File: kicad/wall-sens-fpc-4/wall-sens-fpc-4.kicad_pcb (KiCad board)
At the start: 2 copper layers, 51.5 x 19.7 mm, 32 parts, among them J1 10x0.5mm FPC, Q1 PT100MF0MP, Q2 PT100MF0MP, Q3 PT100MF0MP, Q4 PT100MF0MP, Q5 BC817, Q6 SSM3K122TU, Q7 BC817, Q8 SSM3K122TU

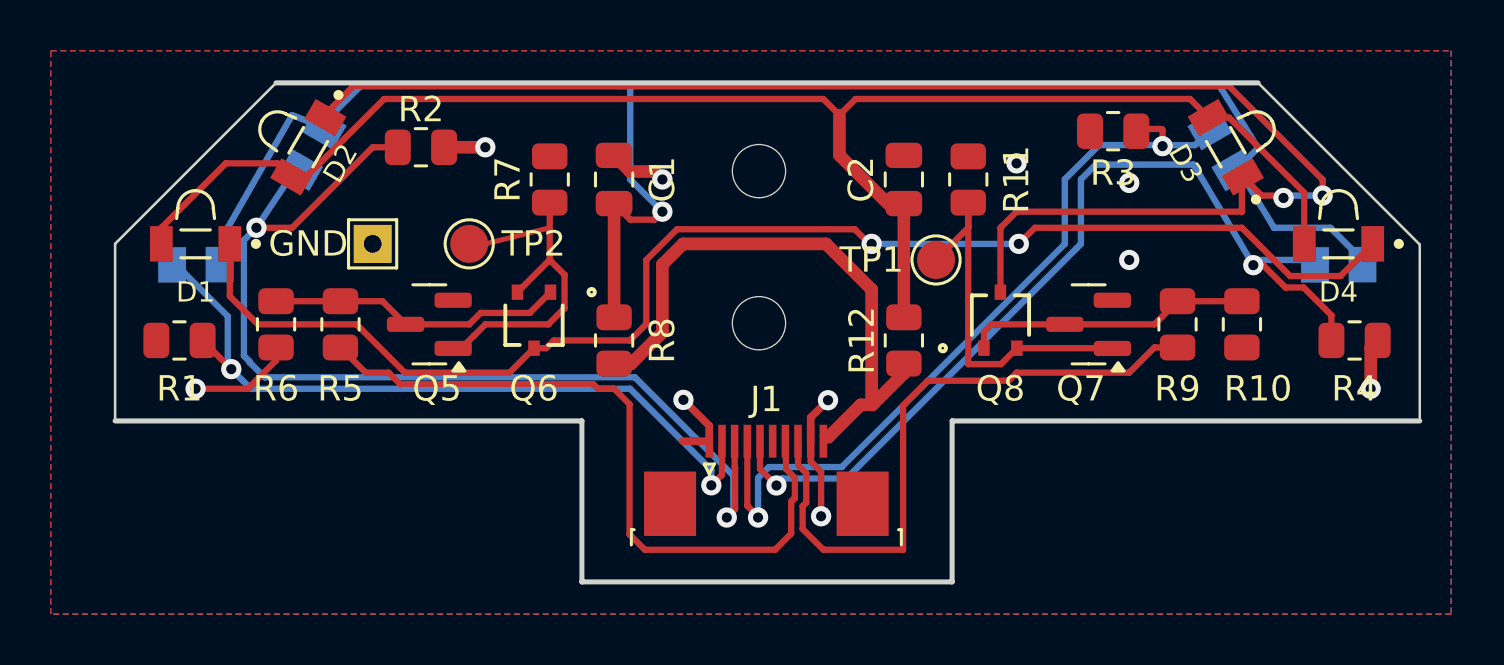
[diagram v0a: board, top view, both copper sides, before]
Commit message: New version of wall-follower for full size. Add new design Half-Monty-2
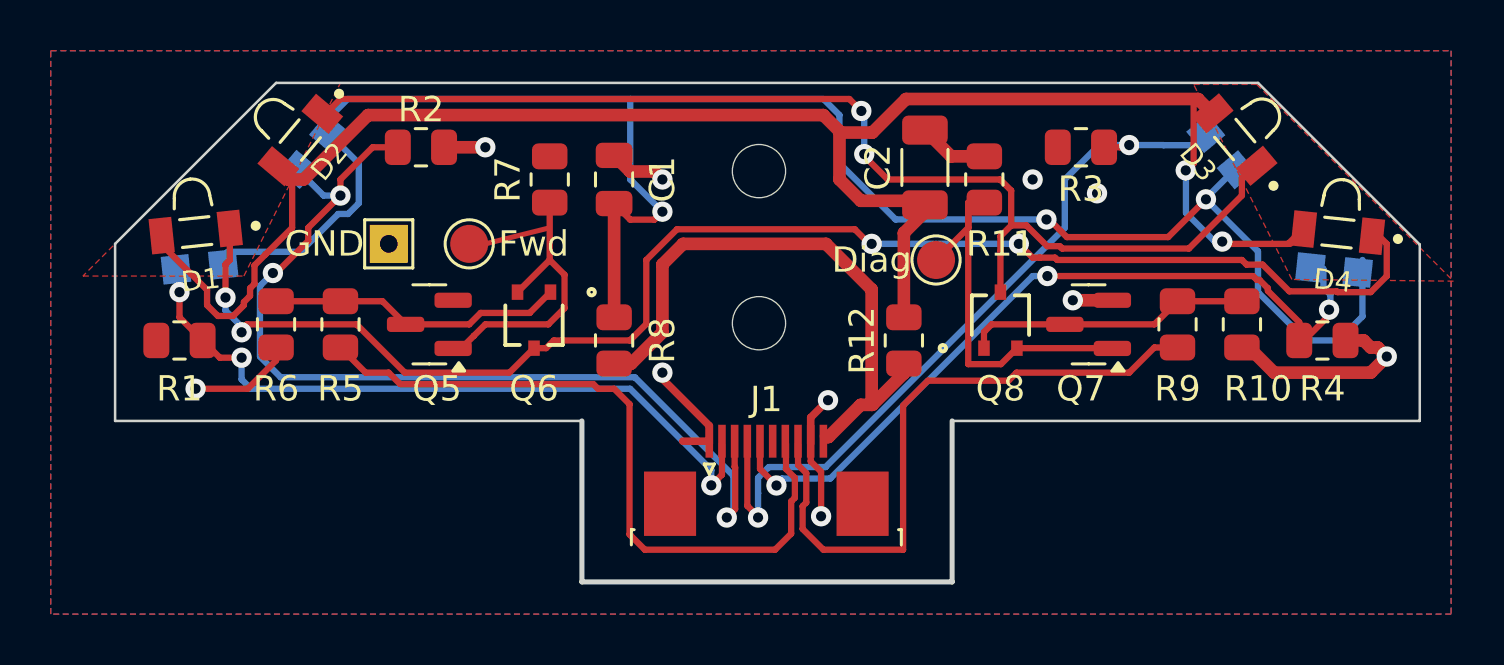
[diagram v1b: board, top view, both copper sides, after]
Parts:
- C2: value 22uF -> 47uF; footprint Capacitor_SMD:C_0805_2012Metric -> Capacitor_SMD:C_1206_3216Metric
- moved R3 1.42 mm to (164.5, 99.1)
- moved R4 1.27 mm to (174.0, 106.7)
- moved C2 0.96 mm to (158.3, 99.9)
- moved R11 0.63 mm to (160.7, 100.3)
- moved TP3 0.63 mm to (137.2, 102.9)
- moved D1 0.47 mm to (129.5, 102.4), turned to -174 degrees
- moved D3 0.47 mm to (170.5, 98.8), turned to 130 degrees
- moved D4 0.44 mm to (174.6, 102.4), turned to 174 degrees
- moved D2 0.43 mm to (133.7, 98.8), turned to -130 degrees
- moved Q4 0.21 mm to (174.5, 103.6), turned to 174 degrees
- moved Q1 0.12 mm to (129.7, 103.5), turned to -174 degrees
- turned Q2 to -130 degrees
- turned Q3 to 130 degrees
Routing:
- net Net-(D2-K): track 59.9 -> 46.6 mm
- net Net-(D1-A): track 61.7 -> 74.7 mm, vias 0 -> 2
- net GND: track 18.4 -> 30.4 mm
- net Net-(Q1-C): track 67.4 -> 74.7 mm, vias 1 -> 3
- net A3: track 37.1 -> 31.6 mm, vias 2 -> 3
- net Net-(D1-K): track 54.0 -> 57.7 mm, vias 2 -> 4
- net A1: track 41.1 -> 38.8 mm, vias 2 -> 3
- net A2: track 31.6 -> 30.5 mm
- net A0: track 29.9 -> 29.0 mm, vias 2 -> 3
- net Net-(Q7-B): track 15.1 -> 15.7 mm
- added copper zone on F.Cu, net (none)

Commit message: Update component values after prototype assembly
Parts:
- C1: value 100nF -> 2.2uF
- R1, R4: value 1k5 -> 510R
- R12: value 22R -> 20R
- R2, R3: value 2k2 -> 680R
- R8: value 220R -> 15R
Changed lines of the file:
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@@
 			)
 		)
-		(property "Value" "2k2"
+		(property "Value" "680R"
 			(at 0 1.65 0)
 			(layer "F.Fab")
@@
 			)
 		)
-		(property "Value" "2k2"
+		(property "Value" "680R"
 			(at 0 1.65 0)
 			(layer "F.Fab")
@@
 			)
 		)
-		(property "Value" "1k5"
+		(property "Value" "510R"
 			(at 0 1.65 0)
 			(layer "F.Fab")
@@
 			)
 		)
-		(property "Value" "220R"
+		(property "Value" "15R"
 			(at 0 1.65 90)
 			(layer "F.Fab")
@@
 			)
 		)
-		(property "Value" "22R"
+		(property "Value" "20R"
 			(at 0 1.65 90)
 			(layer "F.Fab")
@@
 			)
 		)
-		(property "Value" "1k5"
+		(property "Value" "510R"
 			(at 0 1.65 0)
 			(layer "F.Fab")
@@
 			)
 		)
-		(property "Value" "100nF"
+		(property "Value" "2.2uF"
 			(at 0 1.68 90)
 			(layer "F.Fab")
